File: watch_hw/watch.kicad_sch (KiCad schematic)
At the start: 10 parts, among them J1 USB_C_Receptacle_USB2.0, M1 VZ43FC1B5640005L, Q1 DMN65D8LFB, SW1 TL6340AF160Q, SW2 TL6340AF160Q

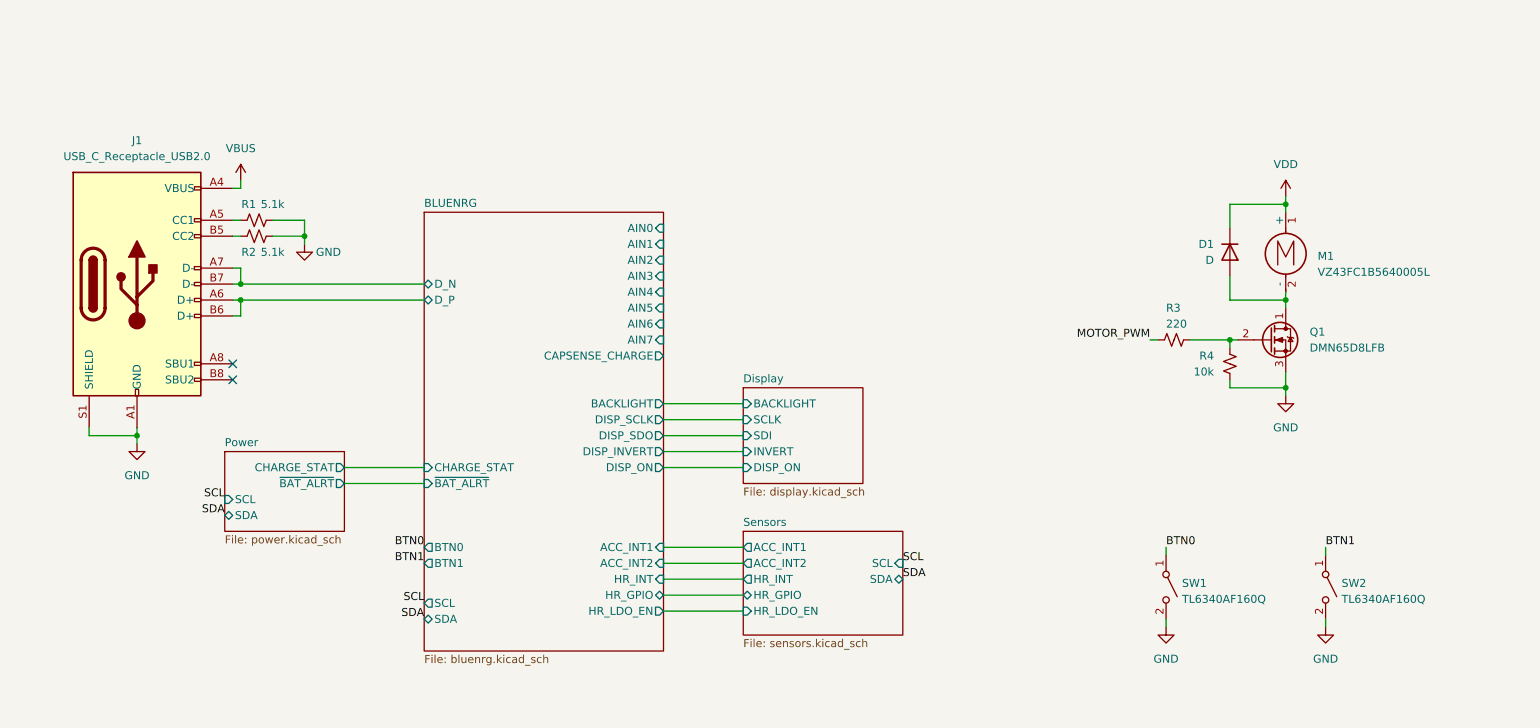
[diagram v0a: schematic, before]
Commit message: Finalize (?) part selection, start layout
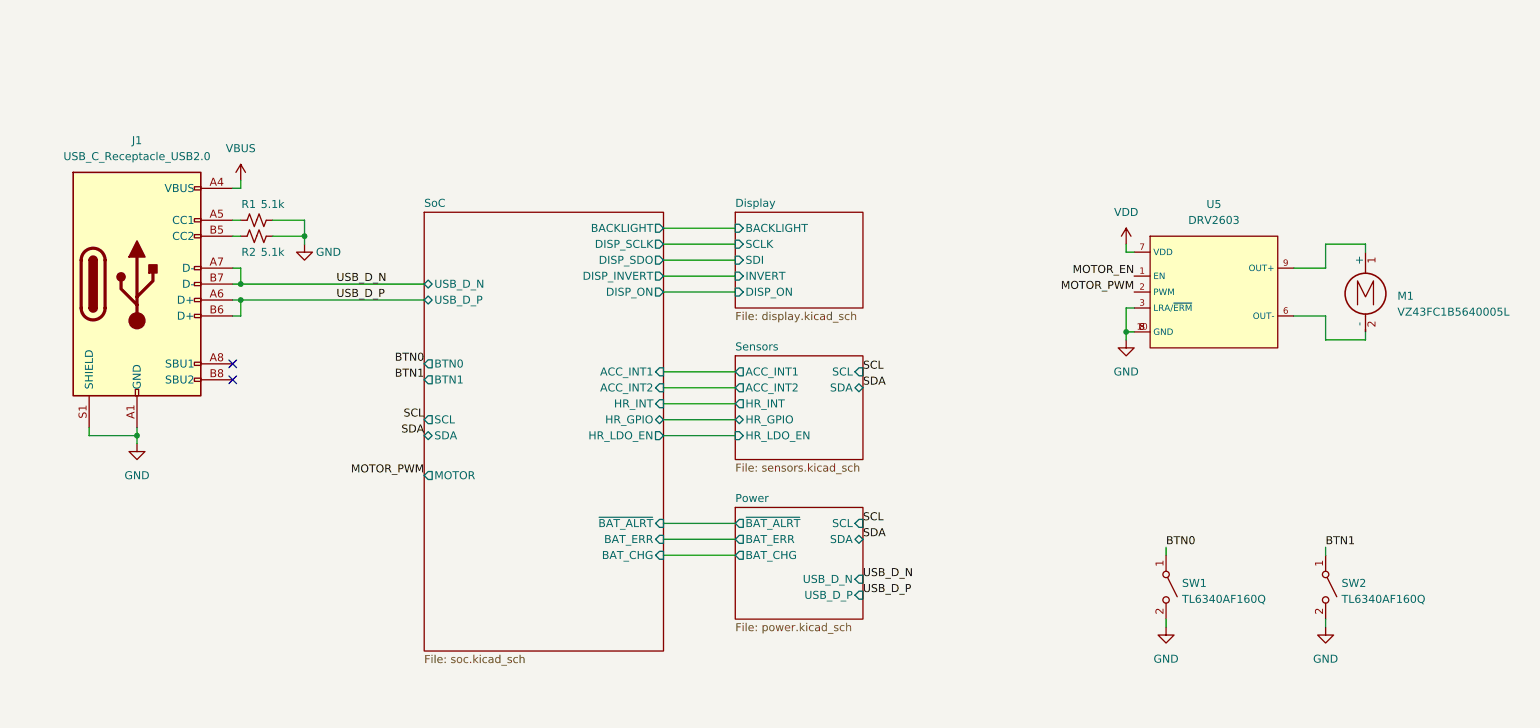
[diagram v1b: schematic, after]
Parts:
- removed D1: D, Diode_SMD:D_0603_1608Metric_Pad1.05x0.95mm_HandSolder, symbol Device:D
- removed Q1: DMN65D8LFB, Package_DFN_QFN:Diodes_DFN1006-3, symbol Device:Q_NMOS_DGS
- removed R3: 220, Resistor_SMD:R_0402_1005Metric_Pad0.72x0.64mm_HandSolder, symbol Device:R_Small_US
- removed R4: 10k, Resistor_SMD:R_0402_1005Metric_Pad0.72x0.64mm_HandSolder, symbol Device:R_Small_US
- added U5: DRV2603, watch:DRV2603RUN, symbol watch:DRV2603
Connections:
- net GND: now also U5.10 (GND), U5.3 (LRA/~{ERM}), U5.5 (GND), U5.8 (GND)
- net MOTOR_PWM: now also U5.2 (PWM)
- net VDD: now also U5.7 (VDD); no longer M1.1 (+)
- net at M1.2 (-): now also U5.6 (OUT-)
- net SoC/D_N renamed USB_D_N
- net SoC/D_P renamed USB_D_P
- new net: M1.1 (+), U5.9 (OUT+)
- new net MOTOR_EN: U5.1 (EN)
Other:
- sheet BLUENRG renamed SoC
- sheet Power ports: added BAT_CHG, BAT_ERR, USB_D_N, USB_D_P; removed CHARGE_STAT
- sheet SoC: file bluenrg.kicad_sch -> soc.kicad_sch
- sheet SoC ports: added BAT_CHG, BAT_ERR, MOTOR, USB_D_N, USB_D_P; removed AIN0, AIN1, AIN2, AIN3, AIN4, AIN5, AIN6, AIN7, CAPSENSE_CHARGE, CHARGE_STAT, D_N, D_P
- moved on the sheet: M1

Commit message: Routing progress
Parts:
- added C26: 0.1uF, Capacitor_SMD:C_0402_1005Metric_Pad0.74x0.62mm_HandSolder, symbol Device:C_Small
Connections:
- net GND: now also C26.2
- net VDD: now also C26.1
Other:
- sheet Display ports: added DISP_CS; removed DISP_ON, INVERT
- sheet Sensors ports: added none; removed HR_GPIO, HR_LDO_EN
- sheet SoC ports: added DISP_CS, MOTOR_EN; removed DISP_INVERT, DISP_ON, HR_GPIO, HR_LDO_EN
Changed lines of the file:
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@@
 (kicad_sch (version 20230121) (generator eeschema)
   (paper "A4")
+  (junction (at 191.77 67.31) (diameter 0) (color 0 0 0 0)
+  )
   (junction (at 207.01 80.01) (diameter 0) (color 0 0 0 0)
   )
@@
     (stroke (width 0) (type default))
   )
-  (wire (pts (xy 207.01 66.04) (xy 207.01 67.31))
+  (wire (pts (xy 191.77 66.04) (xy 191.77 67.31))
     (stroke (width 0) (type default))
   )
@@
     (stroke (width 0) (type default))
   )
+  (wire (pts (xy 133.35 113.03) (xy 144.78 113.03))
+    (stroke (width 0) (type default))
+  )
+  (wire (pts (xy 238.76 66.04) (xy 245.11 66.04))
+    (stroke (width 0) (type default))
+  )
+  (wire (pts (xy 66.04 74.93) (xy 95.25 74.93))
+    (stroke (width 0) (type default))
+  )
+  (wire (pts (xy 64.77 74.93) (xy 66.04 74.93))
+    (stroke (width 0) (type default))
+  )
+  (wire (pts (xy 238.76 114.3) (xy 238.76 115.57))
+    (stroke (width 0) (type default))
+  )
+  (wire (pts (xy 208.28 76.2) (xy 207.01 76.2))
+    (stroke (width 0) (type default))
+  )
+  (wire (pts (xy 207.01 80.01) (xy 208.28 80.01))
+    (stroke (width 0) (type default))
+  )
+  (wire (pts (xy 76.2 62.23) (xy 71.12 62.23))
+    (stroke (width 0) (type default))
+  )
+  (wire (pts (xy 191.77 67.31) (xy 191.77 68.58))
+    (stroke (width 0) (type default))
+  )
+  (wire (pts (xy 238.76 77.47) (xy 238.76 81.28))
+    (stroke (width 0) (type default))
+  )
+  (wire (pts (xy 213.36 114.3) (xy 213.36 115.57))
+    (stroke (width 0) (type default))
+  )
   (wire (pts (xy 133.35 71.12) (xy 144.78 71.12))
     (stroke (width 0) (type default))
   )
-  (wire (pts (xy 133.35 113.03) (xy 144.78 113.03))
-    (stroke (width 0) (type default))
-  )
-  (wire (pts (xy 238.76 66.04) (xy 245.11 66.04))
-    (stroke (width 0) (type default))
-  )
-  (wire (pts (xy 133.35 96.52) (xy 144.78 96.52))
-    (stroke (width 0) (type default))
-  )
-  (wire (pts (xy 66.04 74.93) (xy 95.25 74.93))
-    (stroke (width 0) (type default))
-  )
-  (wire (pts (xy 64.77 74.93) (xy 66.04 74.93))
-    (stroke (width 0) (type default))
-  )
-  (wire (pts (xy 238.76 114.3) (xy 238.76 115.57))
-    (stroke (width 0) (type default))
-  )
-  (wire (pts (xy 208.28 76.2) (xy 207.01 76.2))
-    (stroke (width 0) (type default))
-  )
-  (wire (pts (xy 207.01 80.01) (xy 208.28 80.01))
-    (stroke (width 0) (type default))
-  )
-  (wire (pts (xy 76.2 62.23) (xy 71.12 62.23))
-    (stroke (width 0) (type default))
-  )
-  (wire (pts (xy 133.35 73.66) (xy 144.78 73.66))
-    (stroke (width 0) (type default))
-  )
-  (wire (pts (xy 238.76 77.47) (xy 238.76 81.28))
-    (stroke (width 0) (type default))
-  )
-  (wire (pts (xy 213.36 114.3) (xy 213.36 115.57))
-    (stroke (width 0) (type default))
-  )
   (wire (pts (xy 133.35 86.36) (xy 144.78 86.36))
     (stroke (width 0) (type default))
@@
     (stroke (width 0) (type default))
   )
-  (wire (pts (xy 207.01 67.31) (xy 208.28 67.31))
+  (wire (pts (xy 191.77 67.31) (xy 208.28 67.31))
     (stroke (width 0) (type default))
   )
@@
     (stroke (width 0) (type default))
   )
-  (wire (pts (xy 133.35 93.98) (xy 144.78 93.98))
-    (stroke (width 0) (type default))
-  )
   (wire (pts (xy 133.35 63.5) (xy 144.78 63.5))
     (stroke (width 0) (type default))
@@
   )
   (wire (pts (xy 207.01 76.2) (xy 207.01 80.01))
+    (stroke (width 0) (type default))
+  )
+  (wire (pts (xy 191.77 73.66) (xy 191.77 74.93))
     (stroke (width 0) (type default))
   )
@@
   )
   (label "SCL" (at 95.25 93.98 180) (fields_autoplaced)
+    (effects (font (size 1.27 1.27)) (justify right bottom))
+  )
+  (label "MOTOR_EN" (at 95.25 105.41 180) (fields_autoplaced)
     (effects (font (size 1.27 1.27)) (justify right bottom))
   )
@@
     )
   )
+  (symbol (lib_id "power:GND") (at 191.77 74.93 0) (unit 1)
+    (in_bom yes) (on_board yes) (dnp no) (fields_autoplaced)
+    (property "Reference" "#PWR062" (at 191.77 81.28 0)
+      (effects (font (size 1.27 1.27)) hide)
+    )
+    (property "Value" "GND" (at 191.77 80.01 0)
+      (effects (font (size 1.27 1.27)))
+    )
+    (property "Footprint" "" (at 191.77 74.93 0)
+      (effects (font (size 1.27 1.27)) hide)
+    )
+    (property "Datasheet" "" (at 191.77 74.93 0)
+      (effects (font (size 1.27 1.27)) hide)
+    )
+    (pin "1")
+    (instances
+      (project "watch"
+        (path "/7f737de8-b7e5-4967-9e9f-b541c91fc2b3"
+          (reference "#PWR062") (unit 1)
+        )
+      )
+    )
+  )
   (symbol (lib_id "Device:R_Small_US") (at 68.58 64.77 90) (unit 1)
     (in_bom yes) (on_board yes) (dnp no)
@@
     )
   )
-  (symbol (lib_id "power:VDD") (at 207.01 66.04 0) (unit 1)
-    (in_bom yes) (on_board yes) (dnp no) (fields_autoplaced)
-    (property "Reference" "#PWR02" (at 207.01 69.85 0)
-      (effects (font (size 1.27 1.27)) hide)
-    )
-    (property "Value" "VDD" (at 207.01 60.96 0)
-      (effects (font (size 1.27 1.27)))
-    )
-    (property "Footprint" "" (at 207.01 66.04 0)
-      (effects (font (size 1.27 1.27)) hide)
-    )
-    (property "Datasheet" "" (at 207.01 66.04 0)
+  (symbol (lib_id "power:VDD") (at 191.77 66.04 0) (unit 1)
+    (in_bom yes) (on_board yes) (dnp no) (fields_autoplaced)
+    (property "Reference" "#PWR02" (at 191.77 69.85 0)
+      (effects (font (size 1.27 1.27)) hide)
+    )
+    (property "Value" "VDD" (at 191.77 60.96 0)
+      (effects (font (size 1.27 1.27)))
+    )
+    (property "Footprint" "" (at 191.77 66.04 0)
+      (effects (font (size 1.27 1.27)) hide)
+    )
+    (property "Datasheet" "" (at 191.77 66.04 0)
       (effects (font (size 1.27 1.27)) hide)
     )
@@
         (path "/7f737de8-b7e5-4967-9e9f-b541c91fc2b3"
           (reference "#PWR03") (unit 1)
+        )
+      )
+    )
+  )
+  (symbol (lib_id "Device:C_Small") (at 191.77 71.12 0) (unit 1)
+    (in_bom yes) (on_board yes) (dnp no)
+    (property "Reference" "C26" (at 185.42 69.85 0)
+      (effects (font (size 1.27 1.27)) (justify left))
+    )
+    (property "Value" "0.1uF" (at 184.15 72.39 0)
+      (effects (font (size 1.27 1.27)) (justify left))
+    )
+    (property "Footprint" "Capacitor_SMD:C_0402_1005Metric_Pad0.74x0.62mm_HandSolder" (at 191.77 71.12 0)
+      (effects (font (size 1.27 1.27)) hide)
+    )
+    (property "Datasheet" "~" (at 191.77 71.12 0)
+      (effects (font (size 1.27 1.27)) hide)
+    )
+    (pin "1")
+    (pin "2")
+    (instances
+      (project "watch"
+        (path "/7f737de8-b7e5-4967-9e9f-b541c91fc2b3"
+          (reference "C26") (unit 1)
         )
       )
@@
       (effects (font (size 1.27 1.27)) (justify left))
     )
-    (pin "INVERT" input (at 144.78 71.12 180)
-      (effects (font (size 1.27 1.27)) (justify left))
-    )
-    (pin "DISP_ON" input (at 144.78 73.66 180)
+    (pin "DISP_CS" input (at 144.78 71.12 180)
       (effects (font (size 1.27 1.27)) (justify left))
     )
@@
       (effects (font (size 1.27 1.27)) (justify right))
     )
-    (pin "DISP_INVERT" output (at 133.35 71.12 0)
-      (effects (font (size 1.27 1.27)) (justify right))
-    )
-    (pin "DISP_ON" output (at 133.35 73.66 0)
-      (effects (font (size 1.27 1.27)) (justify right))
-    )
     (pin "DISP_SCLK" output (at 133.35 66.04 0)
       (effects (font (size 1.27 1.27)) (justify right))
@@
       (effects (font (size 1.27 1.27)) (justify right))
     )
-    (pin "HR_GPIO" bidirectional (at 133.35 93.98 0)
-      (effects (font (size 1.27 1.27)) (justify right))
-    )
     (pin "HR_INT" input (at 133.35 91.44 0)
       (effects (font (size 1.27 1.27)) (justify right))
@@
       (effects (font (size 1.27 1.27)) (justify left))
     )
-    (pin "HR_LDO_EN" output (at 133.35 96.52 0)
-      (effects (font (size 1.27 1.27)) (justify right))
-    )
     (pin "USB_D_N" bidirectional (at 95.25 72.39 180)
       (effects (font (size 1.27 1.27)) (justify left))
@@
     (pin "BAT_CHG" input (at 133.35 115.57 0)
       (effects (font (size 1.27 1.27)) (justify right))
+    )
+    (pin "DISP_CS" output (at 133.35 71.12 0)
+      (effects (font (size 1.27 1.27)) (justify right))
+    )
+    (pin "MOTOR_EN" output (at 95.25 105.41 180)
+      (effects (font (size 1.27 1.27)) (justify left))
     )
     (instances
@@
       (effects (font (size 1.27 1.27)) (justify left))
     )
-    (pin "HR_GPIO" bidirectional (at 144.78 93.98 180)
-      (effects (font (size 1.27 1.27)) (justify left))
-    )
     (pin "SDA" bidirectional (at 165.1 88.9 0)
       (effects (font (size 1.27 1.27)) (justify right))
@@
       (effects (font (size 1.27 1.27)) (justify left))
     )
-    (pin "HR_LDO_EN" input (at 144.78 96.52 180)
-      (effects (font (size 1.27 1.27)) (justify left))
-    )

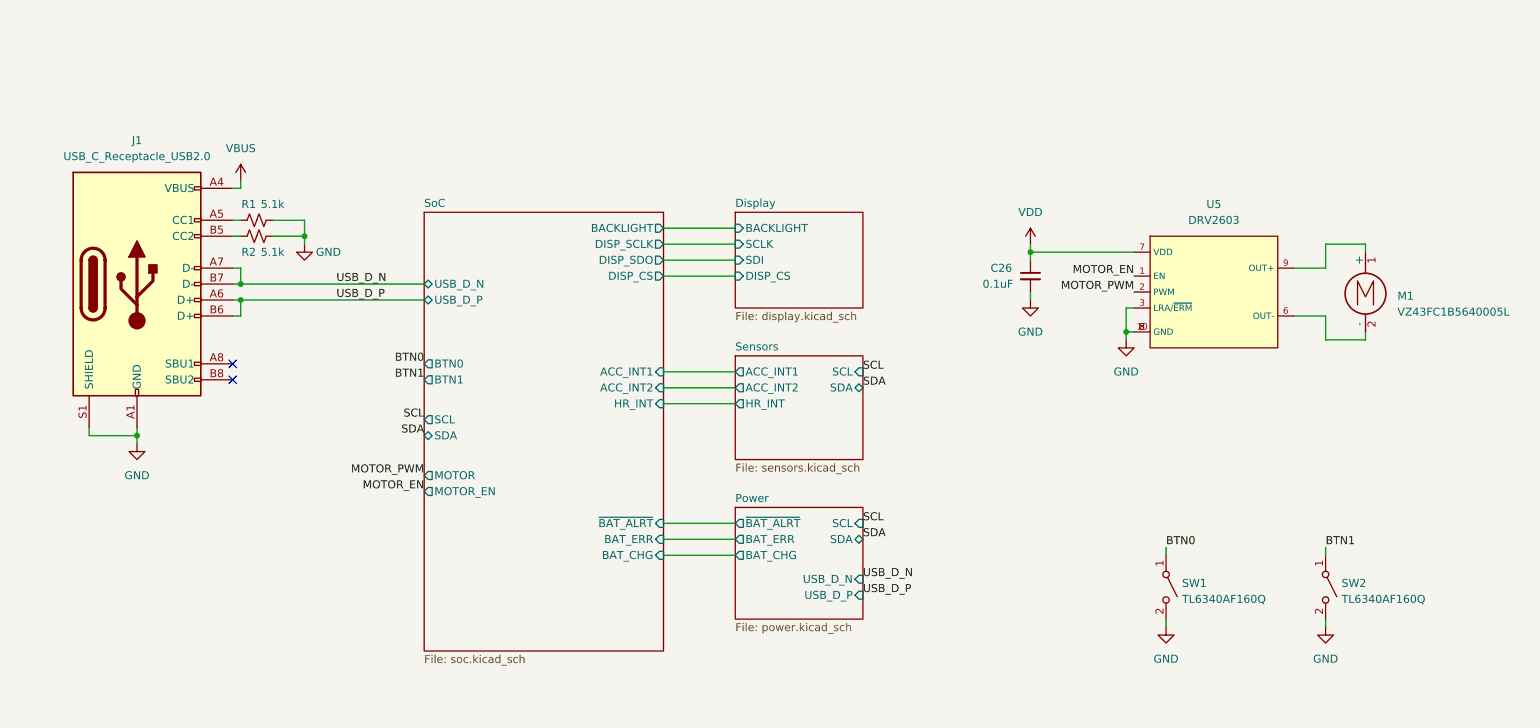
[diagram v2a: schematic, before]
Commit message: Clean up library symbols, update to kicad 8
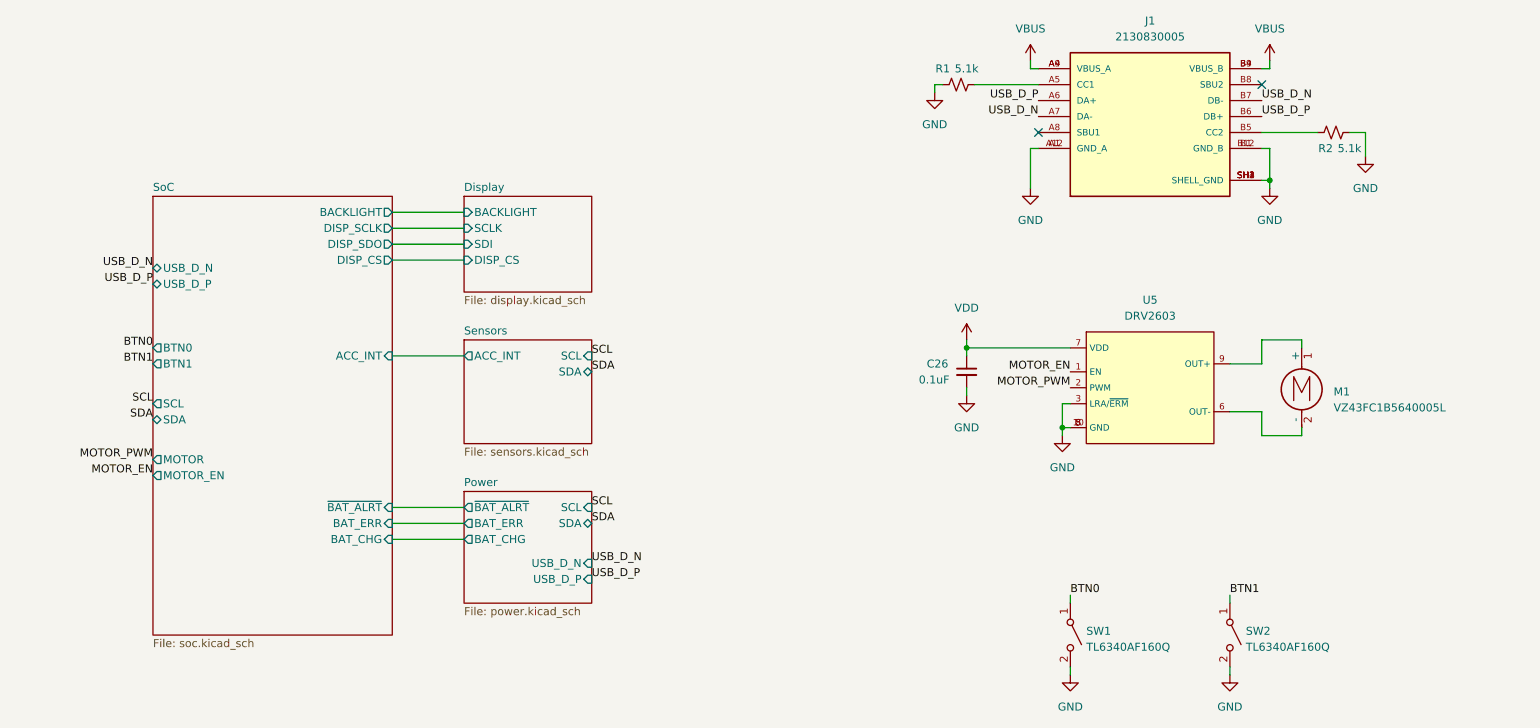
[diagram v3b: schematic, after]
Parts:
- removed J1: USB_C_Receptacle_USB2.0, watch:MOLEX_2130830005, symbol Connector:USB_C_Receptacle_USB2.0
- added J1: 2130830005, watch:MOLEX_2130830005, symbol watch:2130830005
- renumbered R2 to R1, R1 to R2
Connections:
- net GND: now also J1.A1 (GND_A), J1.A12 (GND_A), J1.B1 (GND_B), J1.B12 (GND_B), J1.SH1 (SHELL_GND), J1.SH2 (SHELL_GND), J1.SH3 (SHELL_GND), J1.SH4 (SHELL_GND)
- net USB_D_N: now also J1.A7 (DA-), J1.B7 (DB-)
- net USB_D_P: now also J1.A6 (DA+), J1.B6 (DB+)
- net VBUS: now also J1.A4 (VBUS_A), J1.A9 (VBUS_A), J1.B4 (VBUS_B), J1.B9 (VBUS_B)
- net at R2.1: now also J1.B5 (CC2)
- net at R1.1: now also J1.A5 (CC1)
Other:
- sheet Sensors ports: added ACC_INT; removed ACC_INT1, ACC_INT2, HR_INT
- sheet SoC ports: added ACC_INT; removed ACC_INT1, ACC_INT2, HR_INT
- moved on the sheet: C26, M1, R1, R2, SW1, SW2, U5

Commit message: Start watch v1 layout
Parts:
- removed C26: 0.1uF, Capacitor_SMD:C_0402_1005Metric_Pad0.74x0.62mm_HandSolder, symbol Device:C_Small
- removed J1: 2130830005, watch:MOLEX_2130830005, symbol watch:2130830005
- removed M1: VZ43FC1B5640005L, watch:VZ43FC1B5640005L, symbol Motor:Motor_DC
- removed R1, R2: 5.1k, Resistor_SMD:R_0402_1005Metric_Pad0.72x0.64mm_HandSolder, symbol Device:R_Small_US
- removed U5: DRV2603, watch:DRV2603RUN, symbol watch:DRV2603
- added J1: USB_B_Micro, watch:UJ2-MIBH-4-SMT-TR-67, symbol Connector:USB_B_Micro
- added TP5, TP6: TestPoint, TestPoint:TestPoint_Keystone_5015_Micro_Mini, symbol Connector:TestPoint
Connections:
- net GND: now also J1.5 (GND), J1.6 (Shield)
- net SCL: now also TP6.1
- net SDA: now also TP5.1
- net USB_D_N: now also J1.3 (D+)
- net USB_D_P: now also J1.2 (D-)
- net VBUS: now also J1.1 (VBUS)
- no-connect marks 2 -> 1
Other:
- sheet Display ports: added none; removed BACKLIGHT
- sheet SoC ports: added none; removed BACKLIGHT, MOTOR, MOTOR_EN

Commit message: Route usb data
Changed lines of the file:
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@@
 			)
 		)
-		(pin "BTN0" output
+		(pin "BTN0" input
 			(at 66.04 83.82 180)
 			(effects
@@
 			)
 		)
-		(pin "BTN1" output
+		(pin "BTN1" input
 			(at 66.04 86.36 180)
 			(effects

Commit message: route a bunch, update USB plug board edge
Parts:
- added R7, R8: 10k, Resistor_SMD:R_0402_1005Metric_Pad0.72x0.64mm_HandSolder, symbol Device:R_Small_US
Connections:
- net BTN0: now also R7.2
- net BTN1: now also R8.2
- new net VDD: R7.1, R8.1

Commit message: Add manufacturer/PN fields, select LCSC parts
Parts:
- J1: LCSC (none) -> C22359766
- R7, R8: LCSC (none) -> C25744
- SW1, SW2: LCSC (none) -> C4944967
- TP5, TP6: now not fitted
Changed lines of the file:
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@@
+			)
+		)
+		(property "LCSC" "C25744"
+			(at 223.52 118.11 0)
+			(effects
+				(font
+					(size 1.27 1.27)
+				)
+				(hide yes)
 			)
 		)
@@
 			)
 		)
+		(property "LCSC" "C4944967"
+			(at 198.12 128.27 90)
+			(effects
+				(font
+					(size 1.27 1.27)
+				)
+				(hide yes)
+			)
+		)
 		(pin "1"
 		)
@@
 		(in_bom yes)
 		(on_board yes)
-		(dnp no)
+		(dnp yes)
 		(property "Reference" "TP6"
 			(at 36.068 85.852 0)
@@
 			)
 		)
+		(property "LCSC" "C4944967"
+			(at 223.52 128.27 90)
+			(effects
+				(font
+					(size 1.27 1.27)
+				)
+				(hide yes)
+			)
+		)
 		(pin "1"
 		)
@@
 		(in_bom yes)
 		(on_board yes)
-		(dnp no)
+		(dnp yes)
 		(property "Reference" "TP5"
 			(at 29.718 85.852 0)
@@
 			)
 		)
+		(property "LCSC" "C25744"
+			(at 198.12 118.11 0)
+			(effects
+				(font
+					(size 1.27 1.27)
+				)
+				(hide yes)
+			)
+		)
 		(pin "1"
 		)
@@
 			(at 187.96 69.85 0)
 			(effects
+				(font
+					(size 1.27 1.27)
+				)
+				(hide yes)
+			)
+		)
+		(property "LCSC" "C22359766"
+			(at 187.96 69.85 0)
+			(effects
